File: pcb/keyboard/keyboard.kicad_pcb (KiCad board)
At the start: 2 copper layers, 144.8 x 113 mm, 70 parts, among them J1 Audio-Jack-4, J2 sidebutton, SW1 RESET_SW, U1 Arduino_Pro_Micro

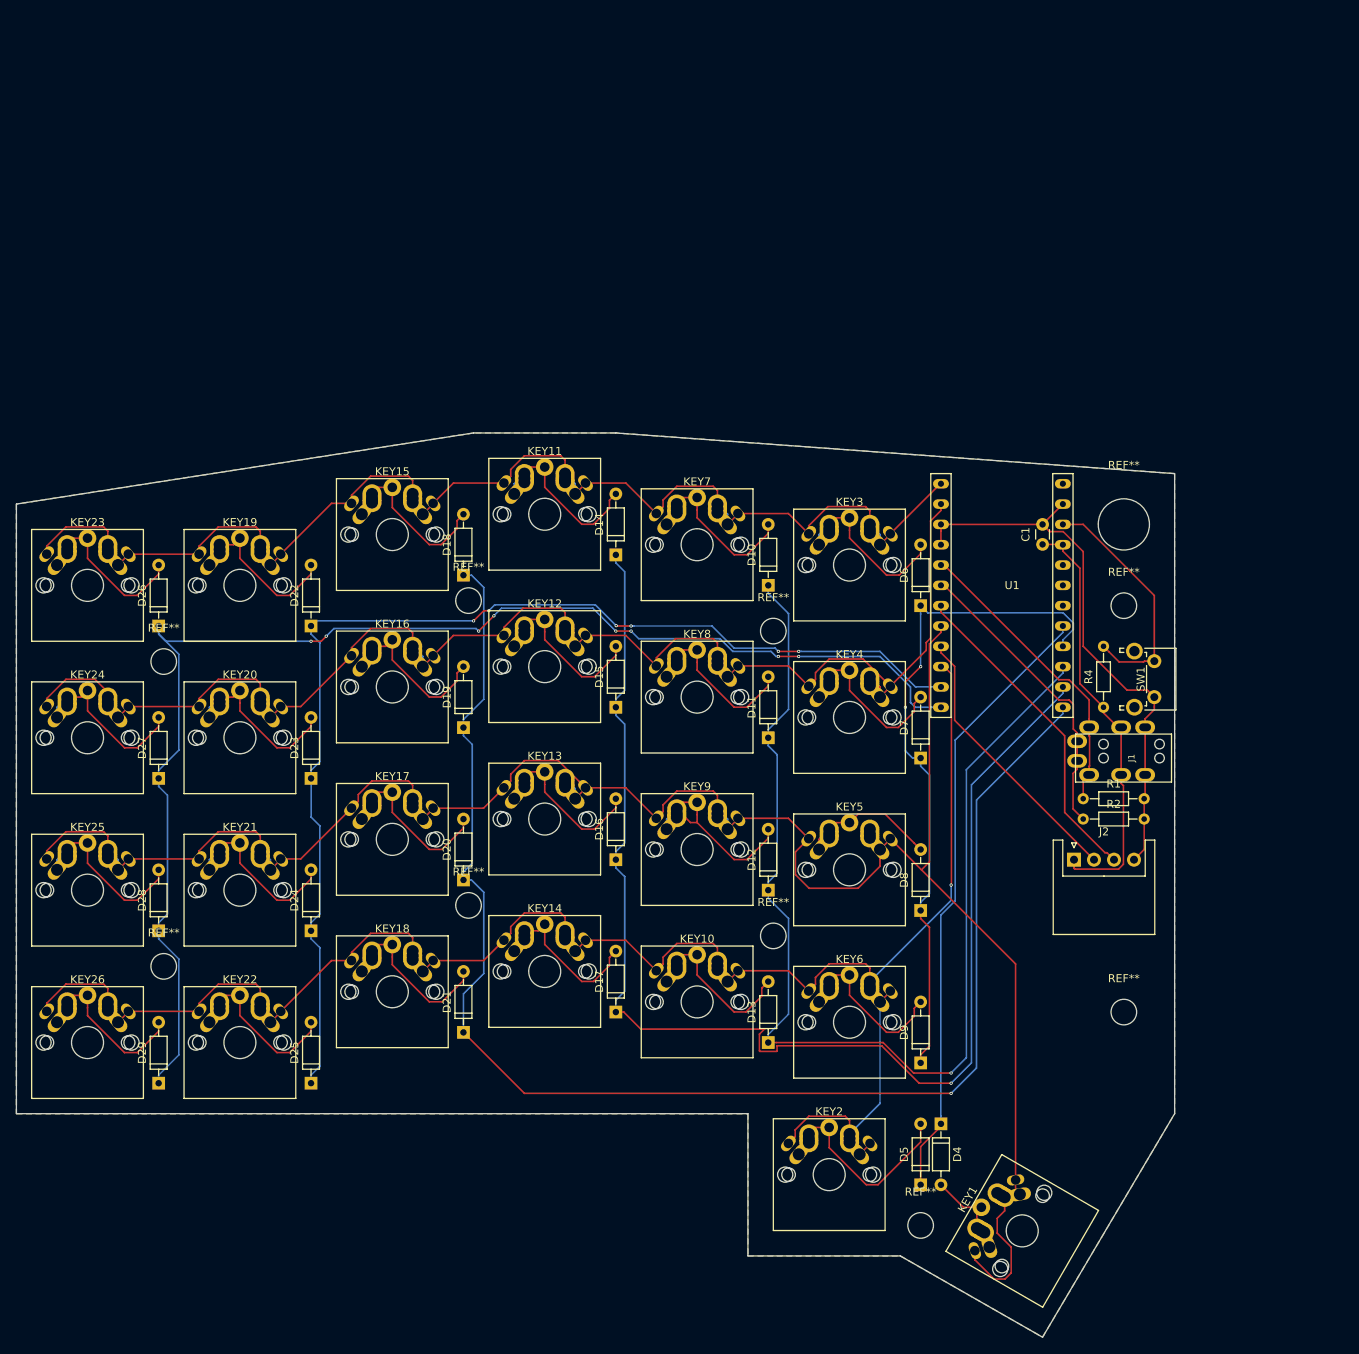
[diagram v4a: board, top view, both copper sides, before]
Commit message: imporve design
 * 小指の担当部の薬指との差をゆるく
 * PCBの切り詰め(強度はプレートで担保)
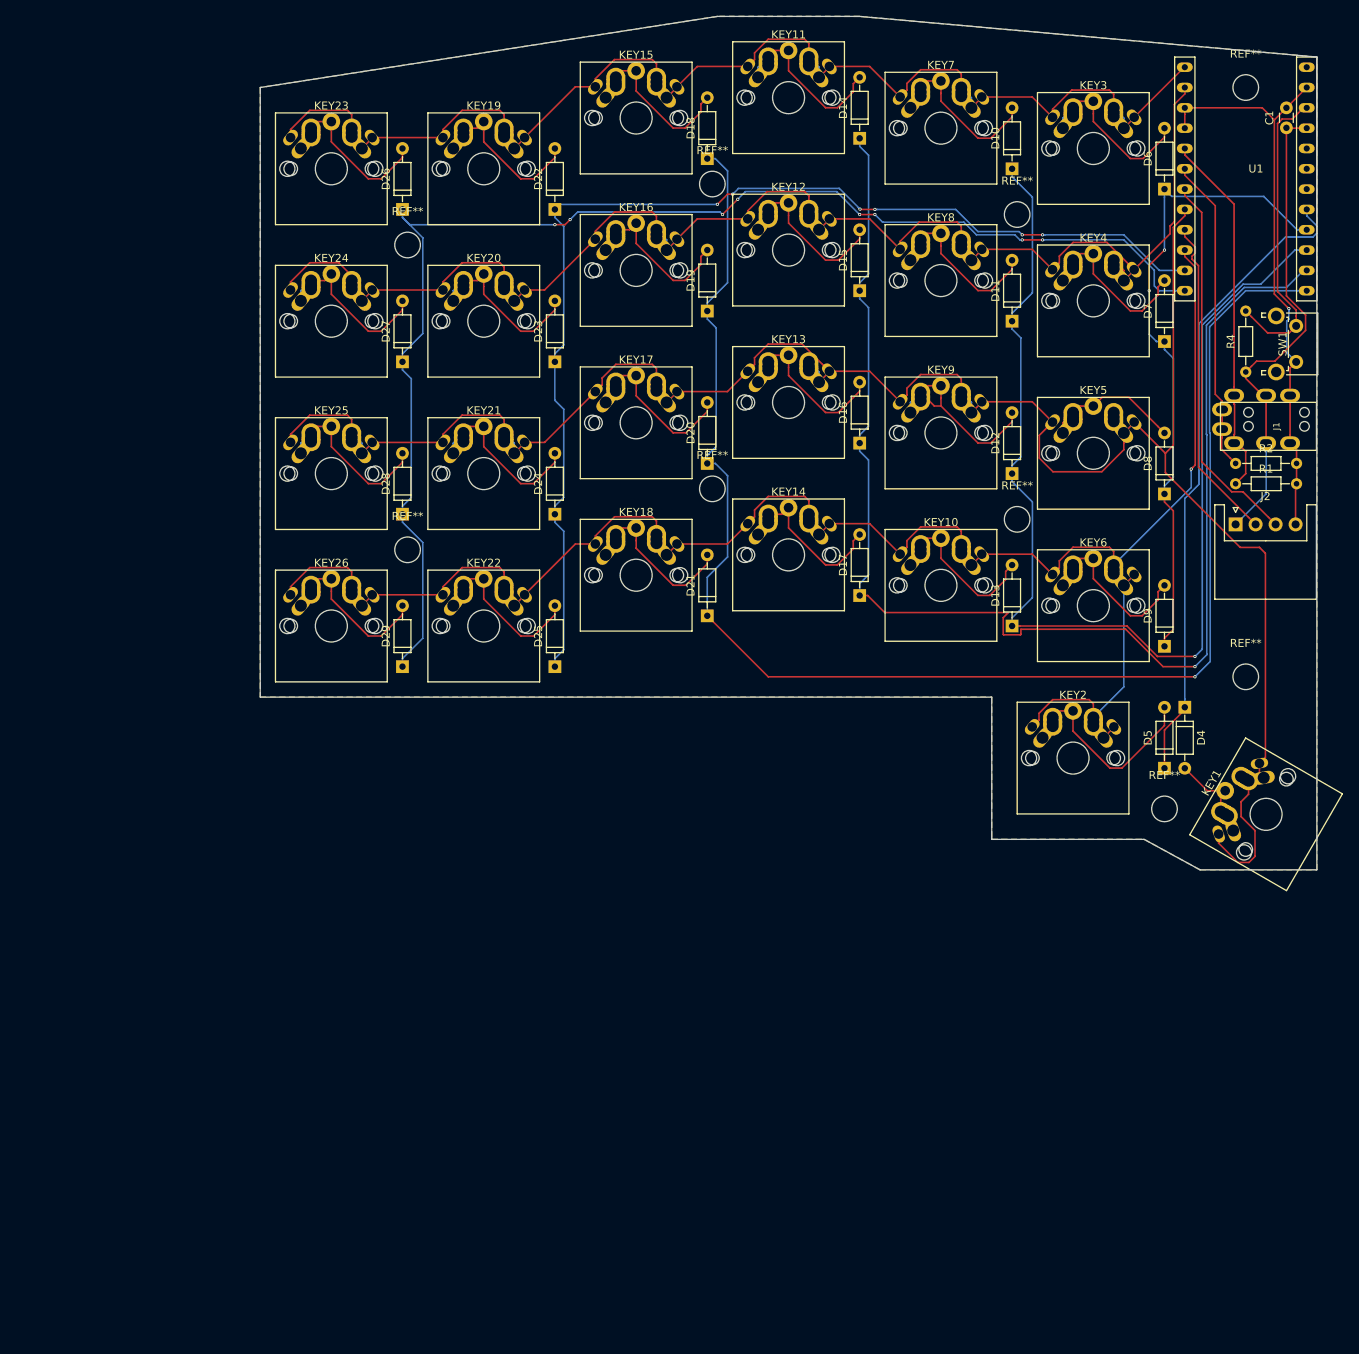
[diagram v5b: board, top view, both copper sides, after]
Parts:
- removed the REF** at (108.0, 54.6)
- moved REF** 66.5 mm to (123.2, 0.00)
- moved D19 60.3 mm to (55.9, 27.9)
- moved D8 60.3 mm to (113.0, 50.8)
- moved D9 60.3 mm to (113.0, 69.8)
- moved KEY1 60.3 mm to (125.7, 90.9)
- moved KEY16 60.3 mm to (47.0, 22.9)
- moved KEY17 60.3 mm to (47.0, 41.9)
- moved KEY5 60.3 mm to (104.1, 45.7)
- moved KEY6 60.3 mm to (104.1, 64.8)
- moved KEY8 60.3 mm to (85.1, 24.1)
- moved REF** 60.3 mm to (113.0, 90.2)
- moved REF** 60.3 mm to (56.5, 12.1)
- moved C1 60.3 mm to (128.3, 5.04)
- moved D11 60.3 mm to (94.0, 29.2)
- moved D12 60.3 mm to (94.0, 48.3)
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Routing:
- net /SDA: track 38.2 -> 46.3 mm
- net /RST: track 30.5 -> 38.5 mm
- net +5V: track 53.4 -> 60.4 mm
- net /Y: track 40.9 -> 47.4 mm
- net /X: track 34.6 -> 40.8 mm
- net /COL4: track 181.6 -> 186.1 mm
- net /COL1: track 84.6 -> 81.0 mm
- net /COL3: track 164.2 -> 167.6 mm
- net /COL0: track 77.2 -> 80.3 mm
- net GND: track 70.1 -> 73.1 mm, vias 0 -> 1
- net /COL2: track 143.3 -> 145.5 mm
- net /ROW2: track 262.5 -> 264.6 mm
- net /SCL: track 38.0 -> 39.9 mm
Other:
- board size 144.8 x 113 mm -> 132.1 x 106.7 mm

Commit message: abolish trancated 値段変わらなくない?
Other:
- board size 132.1 x 106.7 mm -> 134.6 x 111.8 mm
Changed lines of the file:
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@@
     (links 336)
     (no_connects 0)
-    (area -0.913201 -8.940001 139.019593 104.140184)
+    (area -0.050001 -8.940001 134.670001 102.920001)
     (thickness 1.6)
-    (drawings 10)
+    (drawings 11)
     (tracks 886)
     (zones 0)
@@
     )
   )
-  (gr_line (start 132.08 -3.81) (end 132.08 97.79) (layer Edge.Cuts) (width 0.1))
-  (gr_line (start 117.475 97.79) (end 132.08 97.79) (layer Edge.Cuts) (width 0.1))
-  (gr_line (start 110.49 93.98) (end 117.475 97.79) (layer Edge.Cuts) (width 0.1))
+  (gr_line (start 134.62 86.995) (end 132.08 85.09) (layer Edge.Cuts) (width 0.1))
+  (gr_line (start 132.08 -3.81) (end 132.08 85.09) (layer Edge.Cuts) (width 0.1))
+  (gr_line (start 125.73 102.87) (end 134.62 86.995) (layer Edge.Cuts) (width 0.1))
+  (gr_line (start 110.49 93.98) (end 125.73 102.87) (layer Edge.Cuts) (width 0.1))
   (gr_line (start 91.44 93.98) (end 110.49 93.98) (layer Edge.Cuts) (width 0.1))
   (gr_line (start 91.44 76.2) (end 91.44 93.98) (layer Edge.Cuts) (width 0.1))
@@
       (pts
         (xy 132.08 -3.81) (xy 74.93 -8.89) (xy 57.15 -8.89) (xy 0 0) (xy 0 76.2)
-        (xy 91.44 76.2) (xy 91.44 93.98) (xy 110.49 93.98) (xy 117.475 97.79) (xy 132.08 97.79)
-        (xy 132.08 68.58)
+        (xy 91.44 76.2) (xy 91.44 93.98) (xy 110.49 93.98) (xy 125.73 102.87) (xy 134.62 86.995)
+        (xy 132.08 85.09)
       )
     )
@@
     (polygon
       (pts
-        (xy 132.08 97.79) (xy 132.08 68.58) (xy 132.08 -3.81) (xy 74.93 -8.89) (xy 57.15 -8.89)
+        (xy 134.62 86.995) (xy 132.08 85.09) (xy 132.08 -3.81) (xy 74.93 -8.89) (xy 57.15 -8.89)
         (xy 0 0) (xy 0 76.2) (xy 91.44 76.2) (xy 91.44 93.98) (xy 110.49 93.98)
-        (xy 117.475 97.79)
+        (xy 125.73 102.87)
       )
     )

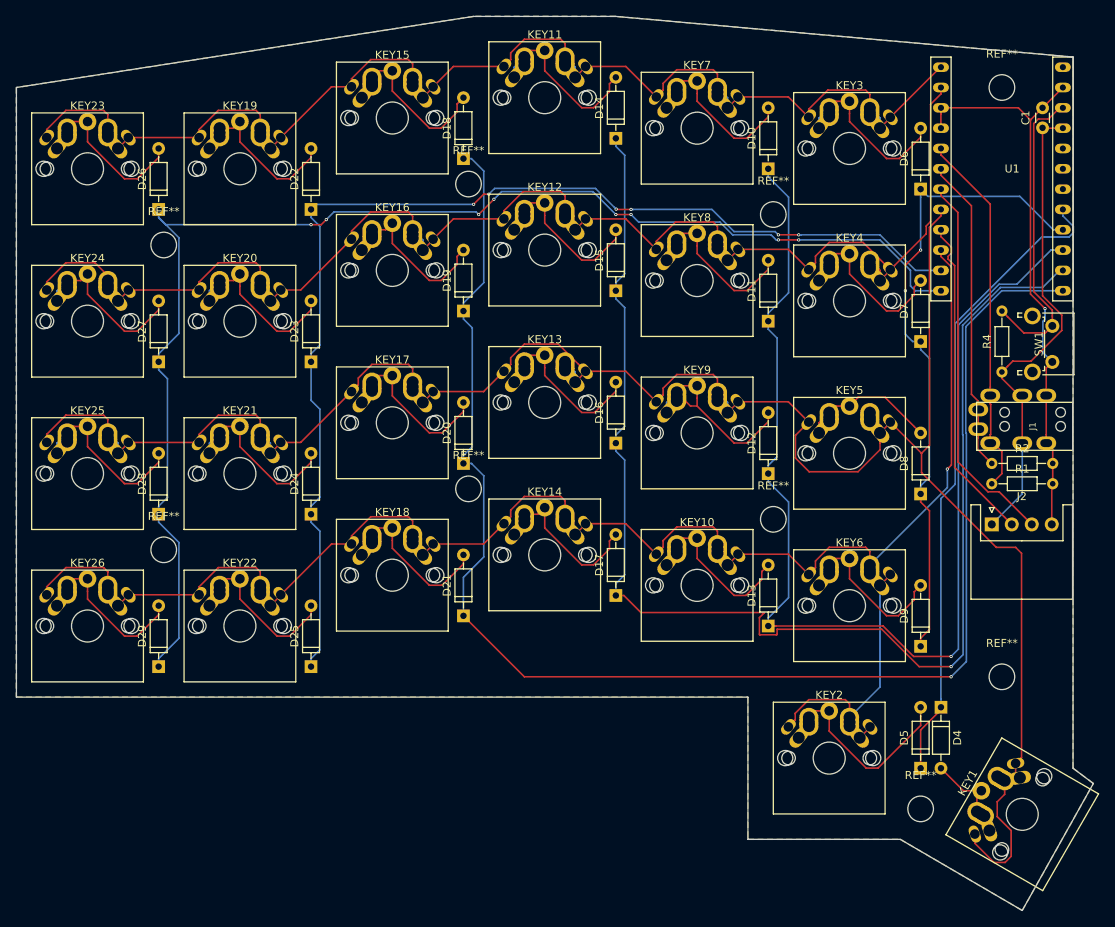
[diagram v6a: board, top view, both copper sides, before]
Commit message: keyboard pcb: add R
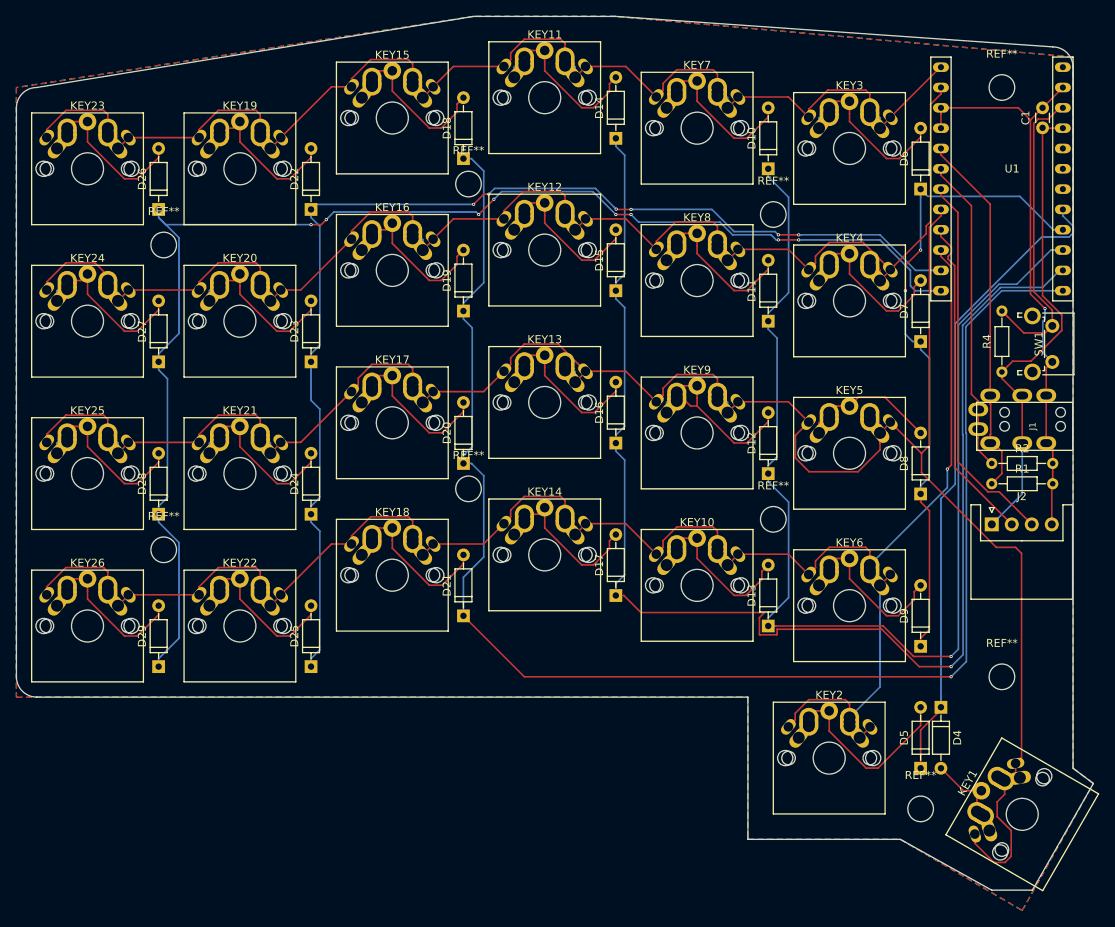
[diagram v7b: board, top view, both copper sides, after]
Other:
- board size 134.6 x 111.8 mm -> 134.6 x 109.2 mm
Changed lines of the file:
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@@
     (links 336)
     (no_connects 0)
-    (area -0.050001 -8.940001 134.670001 102.920001)
+    (area -0.050001 -8.940001 134.670001 100.380001)
     (thickness 1.6)
-    (drawings 11)
+    (drawings 15)
     (tracks 886)
     (zones 0)
@@
     )
   )
+  (gr_line (start 121.92 100.33) (end 127 100.33) (layer Edge.Cuts) (width 0.1))
+  (gr_arc (start 129.54 -2.54) (end 129.54 -5.08) (angle 90) (layer Edge.Cuts) (width 0.1))
+  (gr_arc (start 2.54 2.54) (end 0 2.54) (angle 90) (layer Edge.Cuts) (width 0.1))
+  (gr_arc (start 2.54 73.66) (end 2.54 76.2) (angle 90) (layer Edge.Cuts) (width 0.1))
   (gr_line (start 134.62 86.995) (end 132.08 85.09) (layer Edge.Cuts) (width 0.1))
-  (gr_line (start 132.08 -3.81) (end 132.08 85.09) (layer Edge.Cuts) (width 0.1))
-  (gr_line (start 125.73 102.87) (end 134.62 86.995) (layer Edge.Cuts) (width 0.1))
-  (gr_line (start 110.49 93.98) (end 125.73 102.87) (layer Edge.Cuts) (width 0.1))
+  (gr_line (start 132.08 -2.54) (end 132.08 85.09) (layer Edge.Cuts) (width 0.1))
+  (gr_line (start 127 100.33) (end 134.62 86.995) (layer Edge.Cuts) (width 0.1))
+  (gr_line (start 110.49 93.98) (end 121.92 100.33) (layer Edge.Cuts) (width 0.1))
   (gr_line (start 91.44 93.98) (end 110.49 93.98) (layer Edge.Cuts) (width 0.1))
   (gr_line (start 91.44 76.2) (end 91.44 93.98) (layer Edge.Cuts) (width 0.1))
-  (gr_line (start 0 76.2) (end 91.44 76.2) (layer Edge.Cuts) (width 0.1))
-  (gr_line (start 0 0) (end 0 76.2) (layer Edge.Cuts) (width 0.1))
-  (gr_line (start 57.15 -8.89) (end 0 0) (layer Edge.Cuts) (width 0.1))
+  (gr_line (start 2.54 76.2) (end 91.44 76.2) (layer Edge.Cuts) (width 0.1))
+  (gr_line (start 0 2.54) (end 0 73.66) (layer Edge.Cuts) (width 0.1))
+  (gr_line (start 57.15 -8.89) (end 2.54 0) (layer Edge.Cuts) (width 0.1))
   (gr_line (start 74.93 -8.89) (end 57.15 -8.89) (layer Edge.Cuts) (width 0.1))
-  (gr_line (start 132.08 -3.81) (end 74.93 -8.89) (layer Edge.Cuts) (width 0.1))
+  (gr_line (start 129.54 -5.08) (end 74.93 -8.89) (layer Edge.Cuts) (width 0.1))
   (segment (start 130.81 15.24) (end 130.81 16.0432) (width 0.2032) (layer B.Cu) (net 1))
   (segment (start 128.16839 18.68481) (end 117.344801 29.508399) (width 0.2032) (layer B.Cu) (net 1))
